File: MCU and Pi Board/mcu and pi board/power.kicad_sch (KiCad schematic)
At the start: 38 parts, among them IC1 CSD17578Q3A, IC2 CSD17578Q3A, J1 PJ-002A, J2 ET60S-D04-3-08-D04-X-R1-S, J4 PJ-002A, Q1 BSC010N04LS6ATMA1, Q2 BSC010N04LS6ATMA1, U2 LM3940IMPX-3.3/NOPB, U3 LTC4370CMS_PBF, U5 TPS40305DRCR

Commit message: added some testpoints and some labeling
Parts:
- added TP1, TP2, TP3, TP4, TP5: TestPoint, symbol Connector:TestPoint
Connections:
- net 5V_OUT is gone; now on net +5V: Q1.8, Q2.8, U3.7 (OUT2)
- net +12V: now also TP3.1
- net +3.3V: now also TP4.1
- net +5V: now also TP1.1
- net +6V: now also TP2.1
- net GND: now also TP5.1
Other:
- note added: "12V and 5V Tether In"
- note added: "5V in MUX"
- note added: "5V to 3.3V LDO"
- note added: "Barrel Jack 5V In"
- moved on the sheet: J2

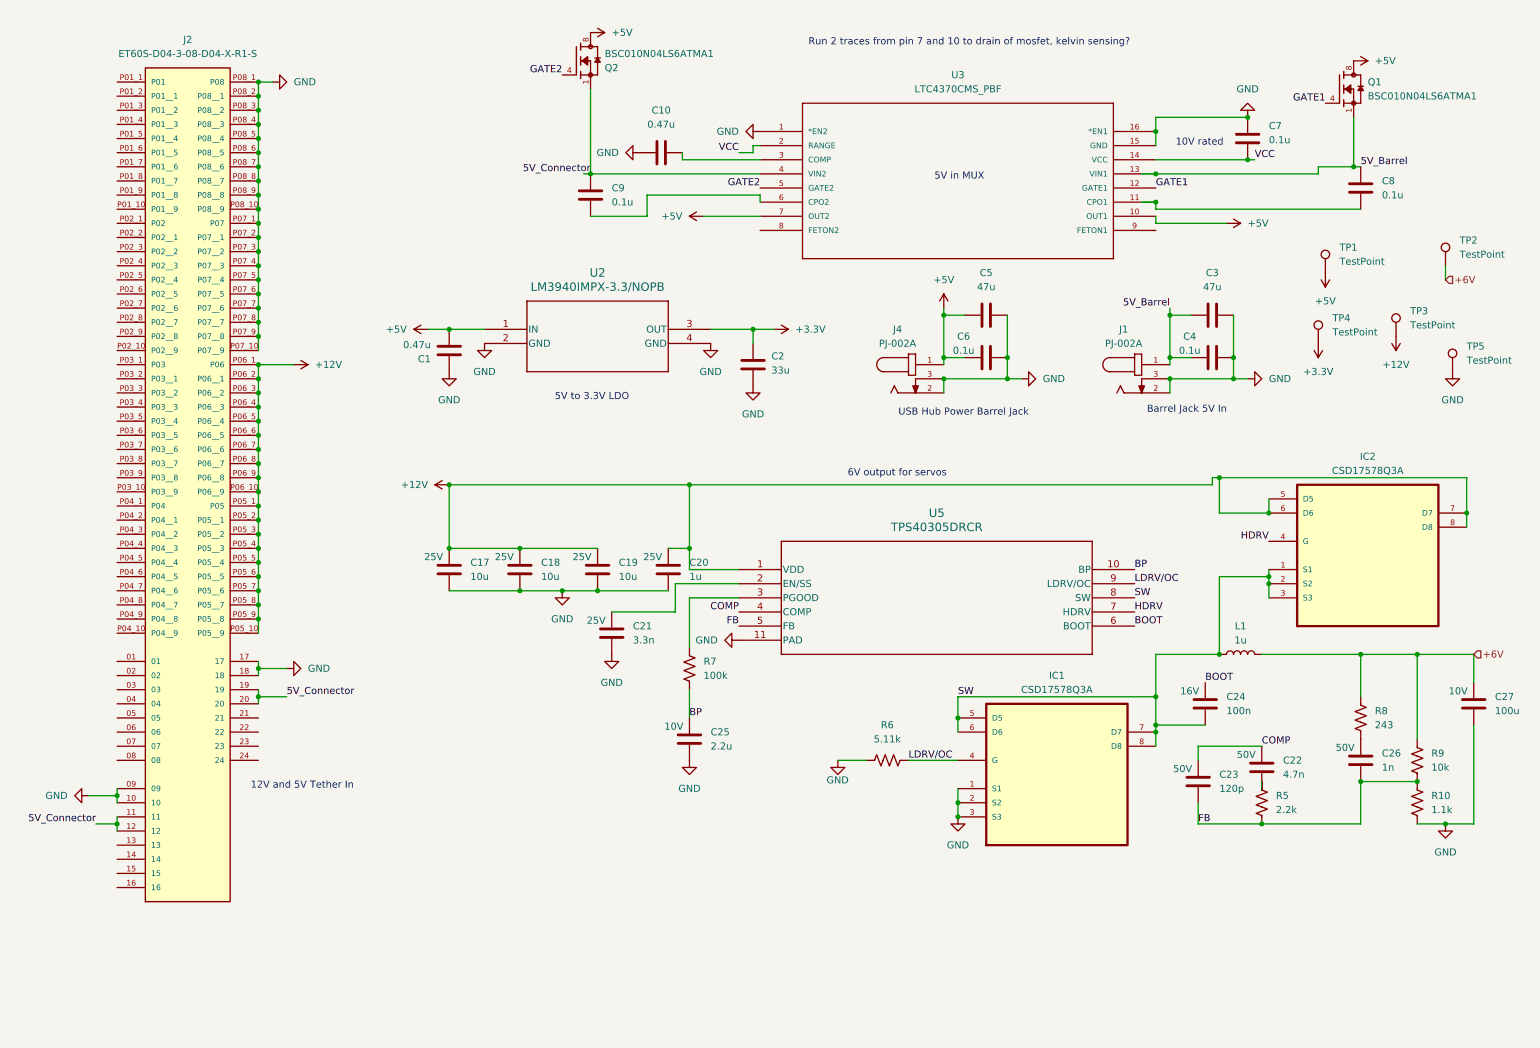
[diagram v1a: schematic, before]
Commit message: added leds and minor fixes
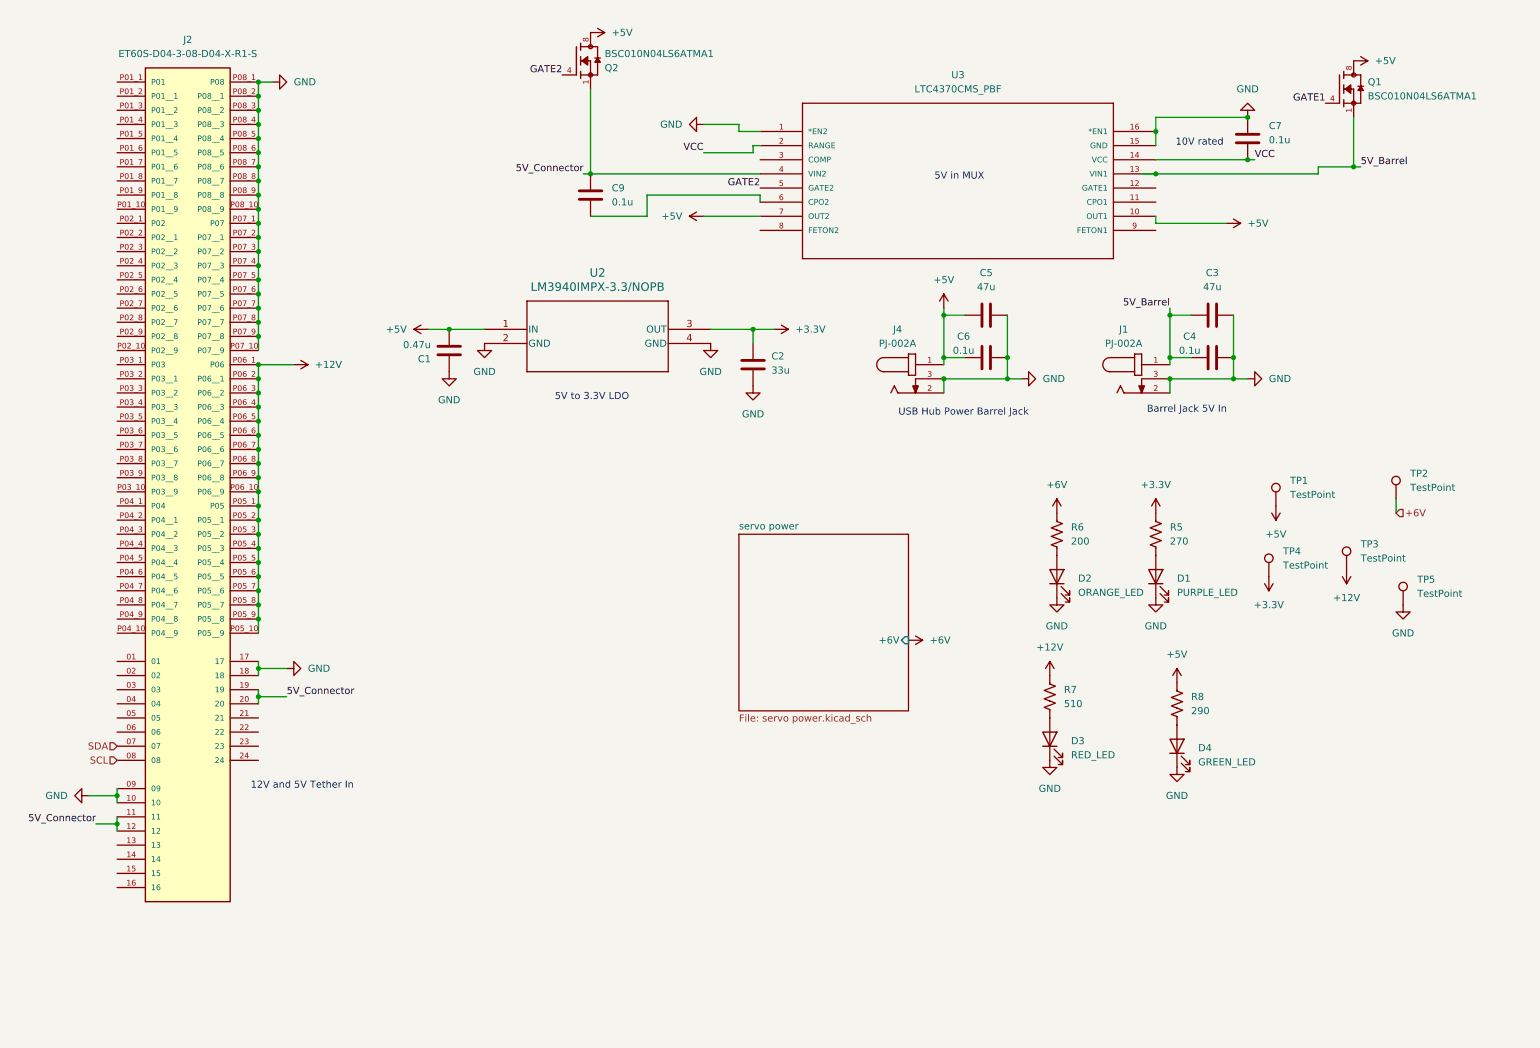
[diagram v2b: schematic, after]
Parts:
- removed C10: 0.47u, symbol Device:C
- removed C17, C18, C19: 10u, symbol Device:C
- removed C20: 1u, symbol Device:C
- removed C21: 3.3n, symbol Device:C
- removed C22: 4.7n, symbol Device:C
- removed C23: 120p, symbol Device:C
- removed C24: 100n, symbol Device:C
- removed C25: 2.2u, symbol Device:C
- removed C26: 1n, symbol Device:C
- removed C27: 100u, symbol Device:C
- removed C8: 0.1u, symbol Device:C
- removed IC1, IC2: CSD17578Q3A, CSD17578Q3A:TRANS_CSD18543Q3A, symbol custom library:CSD17578Q3A
- removed L1: 1u, custom library:IND_XAL6030-102MEC, symbol Device:L
- removed R10: 1.1k, symbol Device:R_US
- removed R9: 10k, symbol Device:R_US
- removed U5: TPS40305DRCR, DRC10_2P4X1P65, symbol custom library:TPS40305DRCR
- added D1: PURPLE_LED, LED_SMD:LED_0201_0603Metric_Pad0.64x0.40mm_HandSolder, symbol Device:LED
- added D2: ORANGE_LED, LED_SMD:LED_0201_0603Metric_Pad0.64x0.40mm_HandSolder, symbol Device:LED
- added D3: RED_LED, LED_SMD:LED_0201_0603Metric_Pad0.64x0.40mm_HandSolder, symbol Device:LED
- added D4: GREEN_LED, LED_SMD:LED_0201_0603Metric_Pad0.64x0.40mm_HandSolder, symbol Device:LED
- R5: value 2.2k -> 270
- R6: value 5.11k -> 200
- R7: value 100k -> 510
- R8: value 243 -> 290
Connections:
- net +12V: now also R7.1
- net +3.3V: now also R5.1
- net +5V: now also R8.1
- net +6V: now also R6.1; no longer R8.1
- net GATE1: no longer U3.12 (GATE1)
- net GND: now also D1.1 (K), D2.1 (K), D3.1 (K), D4.1 (K); no longer R6.1
- net at R8.2: now also D4.2 (A)
- net SDA: now reaches J2.07
- net SCL: now reaches J2.08
- net BP: no longer names the net of R7.2
- net BP: now also D3.2 (A)
- net FB: no longer names the net of R5.2
- net FB: now also D1.2 (A)
- net LDRV/OC: no longer names the net of R6.2
- net LDRV/OC: now also D2.2 (A)
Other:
- added sheet servo power (servo power.kicad_sch)
- note removed: "6V output for servos"
- note removed: "Run 2 traces from pin 7 and 10 to drain of mosfet, kelvin sensing?"
- moved on the sheet: TP1, TP2, TP3, TP4, TP5

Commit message: minor edits
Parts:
- removed C9: 0.1u, symbol Device:C
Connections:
- net GATE1: now also U3.12 (GATE1)
- net GND: now also J2.P01_1 (P01), J2.P01_10 (P01__9), J2.P01_2 (P01__1), J2.P01_3 (P01__2), J2.P01_4 (P01__3), J2.P01_5 (P01__4), J2.P01_6 (P01__5), J2.P01_7 (P01__6), J2.P01_8 (P01__7), J2.P01_9 (P01__8), J2.P02_1 (P02), J2.P02_10 (P02__9), J2.P02_2 (P02__1), J2.P02_3 (P02__2), J2.P02_4 (P02__3), J2.P02_5 (P02__4), J2.P02_6 (P02__5), J2.P02_7 (P02__6), J2.P02_8 (P02__7), J2.P02_9 (P02__8), J2.P03_1 (P03), J2.P03_10 (P03__9), J2.P03_2 (P03__1), J2.P03_3 (P03__2), J2.P03_4 (P03__3), J2.P03_5 (P03__4), J2.P03_6 (P03__5), J2.P03_7 (P03__6), J2.P03_8 (P03__7), J2.P03_9 (P03__8), J2.P04_1 (P04), J2.P04_10 (P04__9), J2.P04_2 (P04__1), J2.P04_3 (P04__2), J2.P04_4 (P04__3), J2.P04_5 (P04__4), J2.P04_6 (P04__5), J2.P04_7 (P04__6), J2.P04_8 (P04__7), J2.P04_9 (P04__8)
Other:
- note added: "Add Decoupling caps"

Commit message: pretty much done i think
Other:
- moved on the sheet: C1, C2, C3, C4, C5, C6, C7, D1, D2, D3, D4, J1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

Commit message: pretty much done
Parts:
- added J13, J14: IPBT-105-H1-T-D-GP, IPBT-105-H1-T-D-GP:SAMTEC_IPBT-105-H1-T-D-GP, symbol custom library:IPBT-105-H1-T-D-GP
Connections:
- net +12V: now also J13.01, J13.02, J13.03, J13.04, J13.05
- net +5V: now also J14.01, J14.02, J14.03, J14.04, J14.05
- net GND: now also J13.06, J13.07, J13.08, J13.09, J13.10, J14.06, J14.07, J14.08, J14.09, J14.10
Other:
- note added: "Tools Power Connectors"

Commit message: started routing
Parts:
- added C10, C9: 0.1u, Capacitor_SMD:C_0603_1608Metric_Pad1.08x0.95mm_HandSolder, symbol Device:C
- added C20, C21: 10u, Capacitor_SMD:C_0805_2012Metric_Pad1.18x1.45mm_HandSolder, symbol Device:C
- added J10: ET60T-D04-0-00-D04-X-R1-S, custom library:SAMTEC_ET60T-D04-0-00-D04-X-R1-S, symbol custom library:ET60T-D04-0-00-D04-X-R1-S
- C1, C4, C6, C7: footprint (none) -> Capacitor_SMD:C_0603_1608Metric_Pad1.08x0.95mm_HandSolder
- C2, C3, C5: footprint (none) -> Capacitor_SMD:C_0805_2012Metric_Pad1.18x1.45mm_HandSolder
- J1, J4: footprint PJ-002A:CUI_PJ-002A -> custom library:CUI_PJ-002A
- J13, J14: footprint IPBT-105-H1-T-D-GP:SAMTEC_IPBT-105-H1-T-D-GP -> custom library:SAMTEC_IPBT-105-H1-T-D-GP
- J2: footprint ET60S-D04-3-08-D04-X-R1-S:SAMTEC_ET60S-D04-3-08-D04-X-R1-S -> custom library:SAMTEC_ET60S-D04-3-08-D04-X-R1-S
- Q1, Q2: footprint BSC010N04LS6ATMA1:TRANS_BSC010N04LS6ATMA1 -> custom library:TRANS_BSC010N04LS6ATMA1
- R5, R6, R7, R8: footprint (none) -> Resistor_SMD:R_0603_1608Metric_Pad0.98x0.95mm_HandSolder
- TP1, TP2, TP3, TP4, TP5: footprint (none) -> TestPoint:TestPoint_Pad_D4.0mm
- U2: footprint MP04A -> custom library:MP04A
- U3: footprint LTC4370CMS_PBF:MSOP-16_MS -> custom library:MSOP-16_MS
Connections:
- net +12V: now also C20.1, C9.1, J10.P03_1 (P03), J10.P03_10 (P03__9), J10.P03_2 (P03__1), J10.P03_3 (P03__2), J10.P03_4 (P03__3), J10.P03_5 (P03__4), J10.P03_6 (P03__5), J10.P03_7 (P03__6), J10.P03_8 (P03__7), J10.P03_9 (P03__8), J10.P04_1 (P04), J10.P04_10 (P04__9), J10.P04_2 (P04__1), J10.P04_3 (P04__2), J10.P04_4 (P04__3), J10.P04_5 (P04__4), J10.P04_6 (P04__5), J10.P04_7 (P04__6), J10.P04_8 (P04__7), J10.P04_9 (P04__8), J10.P06_1 (P06), J10.P06_10 (P06__9), J10.P06_2 (P06__1), J10.P06_3 (P06__2), J10.P06_4 (P06__3), J10.P06_5 (P06__4), J10.P06_6 (P06__5), J10.P06_7 (P06__6), J10.P06_8 (P06__7), J10.P06_9 (P06__8)
- net +5V: now also J10.P05_1 (P05), J10.P05_10 (P05__9), J10.P05_2 (P05__1), J10.P05_3 (P05__2), J10.P05_4 (P05__3), J10.P05_5 (P05__4), J10.P05_6 (P05__5), J10.P05_7 (P05__6), J10.P05_8 (P05__7), J10.P05_9 (P05__8)
- net 5V_Connector: now also C10.1, C21.1
- net GND: now also C10.2, C20.2, C21.2, C9.2, J10.P01_1 (P01), J10.P01_10 (P01__9), J10.P01_2 (P01__1), J10.P01_3 (P01__2), J10.P01_4 (P01__3), J10.P01_5 (P01__4), J10.P01_6 (P01__5), J10.P01_7 (P01__6), J10.P01_8 (P01__7), J10.P01_9 (P01__8), J10.P02_1 (P02), J10.P02_10 (P02__9), J10.P02_2 (P02__1), J10.P02_3 (P02__2), J10.P02_4 (P02__3), J10.P02_5 (P02__4), J10.P02_6 (P02__5), J10.P02_7 (P02__6), J10.P02_8 (P02__7), J10.P02_9 (P02__8), J10.P07_1 (P07), J10.P07_10 (P07__9), J10.P07_2 (P07__1), J10.P07_3 (P07__2), J10.P07_4 (P07__3), J10.P07_5 (P07__4), J10.P07_6 (P07__5), J10.P07_7 (P07__6), J10.P07_8 (P07__7), J10.P07_9 (P07__8), J10.P08_1 (P08), J10.P08_10 (P08__9), J10.P08_2 (P08__1), J10.P08_3 (P08__2), J10.P08_4 (P08__3), J10.P08_5 (P08__4), J10.P08_6 (P08__5), J10.P08_7 (P08__6), J10.P08_8 (P08__7), J10.P08_9 (P08__8)

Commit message: yeet
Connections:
- net +12V: now also J10.P07_1 (P07), J10.P07_10 (P07__9), J10.P07_2 (P07__1), J10.P07_3 (P07__2), J10.P07_4 (P07__3), J10.P07_5 (P07__4), J10.P07_6 (P07__5), J10.P07_7 (P07__6), J10.P07_8 (P07__7), J10.P07_9 (P07__8), J10.P08_1 (P08), J10.P08_10 (P08__9), J10.P08_2 (P08__1), J10.P08_3 (P08__2), J10.P08_4 (P08__3), J10.P08_5 (P08__4), J10.P08_6 (P08__5), J10.P08_7 (P08__6), J10.P08_8 (P08__7), J10.P08_9 (P08__8); no longer J10.P03_1 (P03), J10.P03_10 (P03__9), J10.P03_2 (P03__1), J10.P03_3 (P03__2), J10.P03_4 (P03__3), J10.P03_5 (P03__4), J10.P03_6 (P03__5), J10.P03_7 (P03__6), J10.P03_8 (P03__7), J10.P03_9 (P03__8), J10.P04_1 (P04), J10.P04_10 (P04__9), J10.P04_2 (P04__1), J10.P04_3 (P04__2), J10.P04_4 (P04__3), J10.P04_5 (P04__4), J10.P04_6 (P04__5), J10.P04_7 (P04__6), J10.P04_8 (P04__7), J10.P04_9 (P04__8)
- net GND: now also J10.P03_1 (P03), J10.P03_10 (P03__9), J10.P03_2 (P03__1), J10.P03_3 (P03__2), J10.P03_4 (P03__3), J10.P03_5 (P03__4), J10.P03_6 (P03__5), J10.P03_7 (P03__6), J10.P03_8 (P03__7), J10.P03_9 (P03__8), J10.P04_1 (P04), J10.P04_10 (P04__9), J10.P04_2 (P04__1), J10.P04_3 (P04__2), J10.P04_4 (P04__3), J10.P04_5 (P04__4), J10.P04_6 (P04__5), J10.P04_7 (P04__6), J10.P04_8 (P04__7), J10.P04_9 (P04__8); no longer J10.P07_1 (P07), J10.P07_10 (P07__9), J10.P07_2 (P07__1), J10.P07_3 (P07__2), J10.P07_4 (P07__3), J10.P07_5 (P07__4), J10.P07_6 (P07__5), J10.P07_7 (P07__6), J10.P07_8 (P07__7), J10.P07_9 (P07__8), J10.P08_1 (P08), J10.P08_10 (P08__9), J10.P08_2 (P08__1), J10.P08_3 (P08__2), J10.P08_4 (P08__3), J10.P08_5 (P08__4), J10.P08_6 (P08__5), J10.P08_7 (P08__6), J10.P08_8 (P08__7), J10.P08_9 (P08__8)
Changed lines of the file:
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@@
 	)
 	(junction
+		(at 129.54 147.32)
+		(diameter 0)
+		(color 0 0 0 0)
+	)
+	(junction
 		(at 55.88 115.57)
 		(diameter 0)
@@
 	)
 	(junction
-		(at 154.94 147.32)
-		(diameter 0)
-		(color 0 0 0 0)
-	)
-	(junction
 		(at 30.48 36.83)
 		(diameter 0)
@@
 	)
 	(junction
+		(at 154.94 147.32)
+		(diameter 0)
+		(color 0 0 0 0)
+	)
+	(junction
 		(at 55.88 64.77)
 		(diameter 0)
@@
 	)
 	(junction
-		(at 129.54 147.32)
-		(diameter 0)
-		(color 0 0 0 0)
-	)
-	(junction
 		(at 154.94 116.84)
 		(diameter 0)
@@
 	)
 	(symbol
-		(lib_id "power:+12V")
-		(at 129.54 147.32 90)
+		(lib_id "Device:LED")
+		(at 77.47 93.98 90)
 		(unit 1)
 		(exclude_from_sim no)
@@
 		(dnp no)
 		(fields_autoplaced yes)
-		(property "Reference" "#PWR0111"
-			(at 133.35 147.32 0)
+		(property "Reference" "D1"
+			(at 81.28 94.2974 90)
 			(effects
 				(font
 					(size 1.27 1.27)
 				)
-				(hide yes)
+				(justify right)
 			)
 		)
-		(property "Value" "+12V"
-			(at 125.73 147.3199 90)
+		(property "Value" "PURPLE_LED"
+			(at 81.28 96.8374 90)
 			(effects
 				(font
 					(size 1.27 1.27)
 				)
-				(justify left)
+				(justify right)
 			)
 		)
-		(property "Footprint" ""
-			(at 129.54 147.32 0)
+		(property "Footprint" "LED_SMD:LED_0201_0603Metric_Pad0.64x0.40mm_HandSolder"
+			(at 77.47 93.98 0)
 			(effects
 				(font
@@
 			)
 		)
-		(property "Datasheet" ""
-			(at 129.54 147.32 0)
+		(property "Datasheet" "~"
+			(at 77.47 93.98 0)
 			(effects
 				(font
@@
 			)
 		)
-		(property "Description" "Power symbol creates a global label with name \"+12V\""
-			(at 129.54 147.32 0)
+		(property "Description" "Light emitting diode"
+			(at 77.47 93.98 0)
+			(effects
+				(font
+					(size 1.27 1.27)
+				)
+				(hide yes)
+			)
+		)
+		(property "Sim.Pins" "1=K 2=A"
+			(at 77.47 93.98 0)
 			(effects
 				(font
@@
 			)
 		)
+		(pin "2"
+		)
 		(pin "1"
 		)
@@
 			(project ""
 				(path "/b20a486a-db1b-4621-abfe-a5d205c676b3/bef0208e-671a-46f7-958e-767cd5c13c2b"
-					(reference "#PWR0111")
+					(reference "D1")
 					(unit 1)
 				)
@@
 	)
 	(symbol
-		(lib_id "Device:LED")
-		(at 77.47 93.98 90)
+		(lib_id "power:+12V")
+		(at 154.94 147.32 270)
 		(unit 1)
 		(exclude_from_sim no)
@@
 		(dnp no)
 		(fields_autoplaced yes)
-		(property "Reference" "D1"
-			(at 81.28 94.2974 90)
-			(effects
-				(font
-					(size 1.27 1.27)
-				)
-				(justify right)
-			)
-		)
-		(property "Value" "PURPLE_LED"
-			(at 81.28 96.8374 90)
+		(property "Reference" "#PWR0114"
+			(at 151.13 147.32 0)
 			(effects
 				(font
 					(size 1.27 1.27)
 				)
-				(justify right)
+				(hide yes)
 			)
 		)
-		(property "Footprint" "LED_SMD:LED_0201_0603Metric_Pad0.64x0.40mm_HandSolder"
-			(at 77.47 93.98 0)
+		(property "Value" "+12V"
+			(at 158.75 147.3199 90)
 			(effects
 				(font
 					(size 1.27 1.27)
 				)
-				(hide yes)
+				(justify left)
 			)
 		)
-		(property "Datasheet" "~"
-			(at 77.47 93.98 0)
+		(property "Footprint" ""
+			(at 154.94 147.32 0)
 			(effects
 				(font
@@
 			)
 		)
-		(property "Description" "Light emitting diode"
-			(at 77.47 93.98 0)
+		(property "Datasheet" ""
+			(at 154.94 147.32 0)
 			(effects
 				(font
@@
 			)
 		)
-		(property "Sim.Pins" "1=K 2=A"
-			(at 77.47 93.98 0)
+		(property "Description" "Power symbol creates a global label with name \"+12V\""
+			(at 154.94 147.32 0)
 			(effects
 				(font
@@
 			)
 		)
-		(pin "2"
-		)
 		(pin "1"
 		)
 		(instances
-			(project ""
+			(project "mcu and pi board"
 				(path "/b20a486a-db1b-4621-abfe-a5d205c676b3/bef0208e-671a-46f7-958e-767cd5c13c2b"
-					(reference "D1")
+					(reference "#PWR0114")
 					(unit 1)
 				)
@@
 	)
 	(symbol
-		(lib_id "power:GND")
-		(at 154.94 147.32 90)
-		(unit 1)
-		(exclude_from_sim no)
-		(in_bom yes)
-		(on_board yes)
-		(dnp no)
-		(fields_autoplaced yes)
-		(property "Reference" "#PWR0114"
-			(at 161.29 147.32 0)
-			(effects
-				(font
-					(size 1.27 1.27)
-				)
-				(hide yes)
-			)
-		)
-		(property "Value" "GND"
-			(at 158.75 147.3199 90)
-			(effects
-				(font
-					(size 1.27 1.27)
-				)
-				(justify right)
-			)
-		)
-		(property "Footprint" ""
-			(at 154.94 147.32 0)
-			(effects
-				(font
-					(size 1.27 1.27)
-				)
-				(hide yes)
-			)
-		)
-		(property "Datasheet" ""
-			(at 154.94 147.32 0)
-			(effects
-				(font
-					(size 1.27 1.27)
-				)
-				(hide yes)
-			)
-		)
-		(property "Description" "Power symbol creates a global label with name \"GND\" , ground"
-			(at 154.94 147.32 0)
-			(effects
-				(font
-					(size 1.27 1.27)
-				)
-				(hide yes)
-			)
-		)
-		(pin "1"
-		)
-		(instances
-			(project ""
-				(path "/b20a486a-db1b-4621-abfe-a5d205c676b3/bef0208e-671a-46f7-958e-767cd5c13c2b"
-					(reference "#PWR0114")
-					(unit 1)
-				)
-			)
-		)
-	)
-	(symbol
 		(lib_id "power:+5V")
 		(at 60.96 52.07 180)
@@
 					(unit 1)
 				)
+			)
+		)
+	)
+	(symbol
+		(lib_id "power:GND")
+		(at 129.54 147.32 270)
+		(unit 1)
+		(exclude_from_sim no)
+		(in_bom yes)
+		(on_board yes)
+		(dnp no)
+		(fields_autoplaced yes)
+		(property "Reference" "#PWR0111"
+			(at 123.19 147.32 0)
+			(effects
+				(font
+					(size 1.27 1.27)
+				)
+				(hide yes)
+			)
+		)
+		(property "Value" "GND"
+			(at 125.73 147.3199 90)
+			(effects
+				(font
+					(size 1.27 1.27)
+				)
+				(justify right)
+			)
+		)
+		(property "Footprint" ""
+			(at 129.54 147.32 0)
+			(effects
+				(font
+					(size 1.27 1.27)
+				)
+				(hide yes)
+			)
+		)
+		(property "Datasheet" ""
+			(at 129.54 147.32 0)
+			(effects
+				(font
+					(size 1.27 1.27)
+				)
+				(hide yes)
+			)
+		)
+		(property "Description" "Power symbol creates a global label with name \"GND\" , ground"
+			(at 129.54 147.32 0)
+			(effects
+				(font
+					(size 1.27 1.27)
+				)
+				(hide yes)
+			)
+		)
+		(pin "1"
+		)
+		(instances
+			(project "mcu and pi board"
+				(path "/b20a486a-db1b-4621-abfe-a5d205c676b3/bef0208e-671a-46f7-958e-767cd5c13c2b"
+					(reference "#PWR0111")
+					(unit 1)
+				)

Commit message: basically done
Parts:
- added TP2, TP6: TestPoint, TestPoint:TestPoint_Pad_D4.0mm, symbol Connector:TestPoint
- renumbered C3 to C1, C1 to C10, C2 to C11, C4 to C2, C7 to C3, C6 to C4, C21 to C6, C10 to C7, C20 to C8, D4 to D1, D1 to D2, D2 to D4, J10 to J14, J13 to J24, J1 to J3, J4 to J5, J14 to J6, Q2 to Q1, Q1 to Q2, R8 to R1, R6 to R16, R5 to R2, R7 to R3, TP4 to TP3, TP3 to TP4, TP2 to TP7, U3 to U1
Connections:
- net GND: now also TP2.1, TP6.1
